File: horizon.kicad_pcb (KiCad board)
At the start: 4 copper layers, 50 x 100 mm, 242 parts, among them IC1 A3909, J1 Micro_SD_Card_Det1, J10 Conn_01x02_Pin, J11 USB_C_Receptacle_USB2.0_16P, J12 Conn_01x04, J13 1x3 servo, J14 1x3 servo, J15 arming terminal, J16 arming terminal, J17 arming terminal, J18 arming terminal, J19 Screw_Terminal_01x02, J2 Conn_02x03_Counter_Clockwise, J20 Screw_Terminal_01x02, J21 Screw_Terminal_01x02, J22 Screw_Terminal_01x02, J23 USB_C_Receptacle_USB2.0_16P, J24 USB_C_Receptacle_USB2.0_16P, J25 Conn_Coaxial, J3 Conn_Coaxial, J4 H9161TR-ND, J5 Screw_Term, J6 1x3 servo, J7 Conn_02x03_Counter_Clockwise, J8 Conn_02x03_Counter_Clockwise, J9 1x3 servo, Q1 IRLML6402, Q10 IRLML6402, Q11 IRLML6402, Q2 DMG2301L, Q3 IRLML6402, Q4 IRLML6402, Q5 IRLML6402, Q6 IRLML6402, Q7 BSS138, Q8 IRLML6402, Q9 IRLML6402, U1 MMCU, U10 LSM6DS3, U11 BGM220SC12WGA2R, U13 LTC4412xS6, U14 TPS61092, U15 AP2112K-3.3, U2 IMU, U3 NMCU, U4 TMCU, U5 LPS22HB, U6 GPS, U7 SX1276, U8 NAND, U9 TPS82130, Y1 Crystal, Y2 32.768kHz

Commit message: Added fill
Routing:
- added copper zone on B.Cu, net GND
- added copper zone on F.Cu, net GND
- added copper zone on In1.Cu, net GND
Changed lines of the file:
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@@
 		(net 315)
+	)
+	(zone
+		(net 2)
+		(net_name "GND")
+		(layers "F.Cu" "B.Cu" "In1.Cu")
+		(hatch edge 0.5)
+		(connect_pads
+			(clearance 0.5)
+		)
+		(min_thickness 0.25)
+		(filled_areas_thickness no)
+		(fill yes
+			(thermal_gap 0.5)
+			(thermal_bridge_width 0.5)
+		)
+		(polygon
+			(pts
+				(xy 76 16) (xy 126 16) (xy 126 116) (xy 76 116)
+			)
+		)
 	)
 	(embedded_fonts no)

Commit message: Started routing for BL
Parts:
- Bluetooth: renamed from U11; moved to B.Cu
- C1, C2, C3, C4, L3, R1, R2: moved to B.Cu
- SMA_BL: renamed from J25; moved to B.Cu
- SMA_GPS: renamed from J3; moved to B.Cu
- moved C20 86.4 mm to (168.3, 64.4)
- moved D2 86.4 mm to (168.2, 66.0)
- moved L1 86.4 mm to (169.3, 59.8)
- moved R11 86.4 mm to (173.5, 55.5)
- moved C4 70.6 mm to (114.0, 80.0), turned to 90 degrees
- moved L3 68.8 mm to (109.5, 79.0)
- moved GPS 64.0 mm to (151.0, 64.0), turned to -90 degrees
- moved Bluetooth 60.5 mm to (101.5, 86.5), turned to 90 degrees
- moved C3 58.6 mm to (97.5, 88.4), turned to 90 degrees
- moved U.FL_RF 56.6 mm to (211.0, 110.5), turned to -90 degrees
- moved C1 56.4 mm to (99.5, 81.6), turned to -90 degrees
- moved C2 54.8 mm to (101.0, 81.6), turned to -90 degrees
- moved R2 50.3 mm to (105.5, 83.9), turned to 90 degrees
- moved R1 49.4 mm to (106.3, 86.1)
- moved SMA_BL 48.9 mm to (101.0, 93.5), turned to -90 degrees
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- renumbered U6 to GPS, J11 to MMCU, U1 to MMCU, J23 to NMCU, U3 to NMCU, U7 to RF, J24 to TMCU, U4 to TMCU, J4 to U.FL_RF
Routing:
- net Net-(J25-In): track 0.00 -> 23.2 mm
- net Net-(U11-ANT_OUT): track 0.00 -> 11.2 mm
- net +3.3V: track 114.1 -> 120.8 mm
- net GND: track 192.9 -> 187.3 mm, vias 99 -> 96
- net Net-(D2-A): track 6.34 -> 10.9 mm, vias 0 -> 1
- net Net-(U11-DECOUPLE): track 0.00 -> 1.41 mm

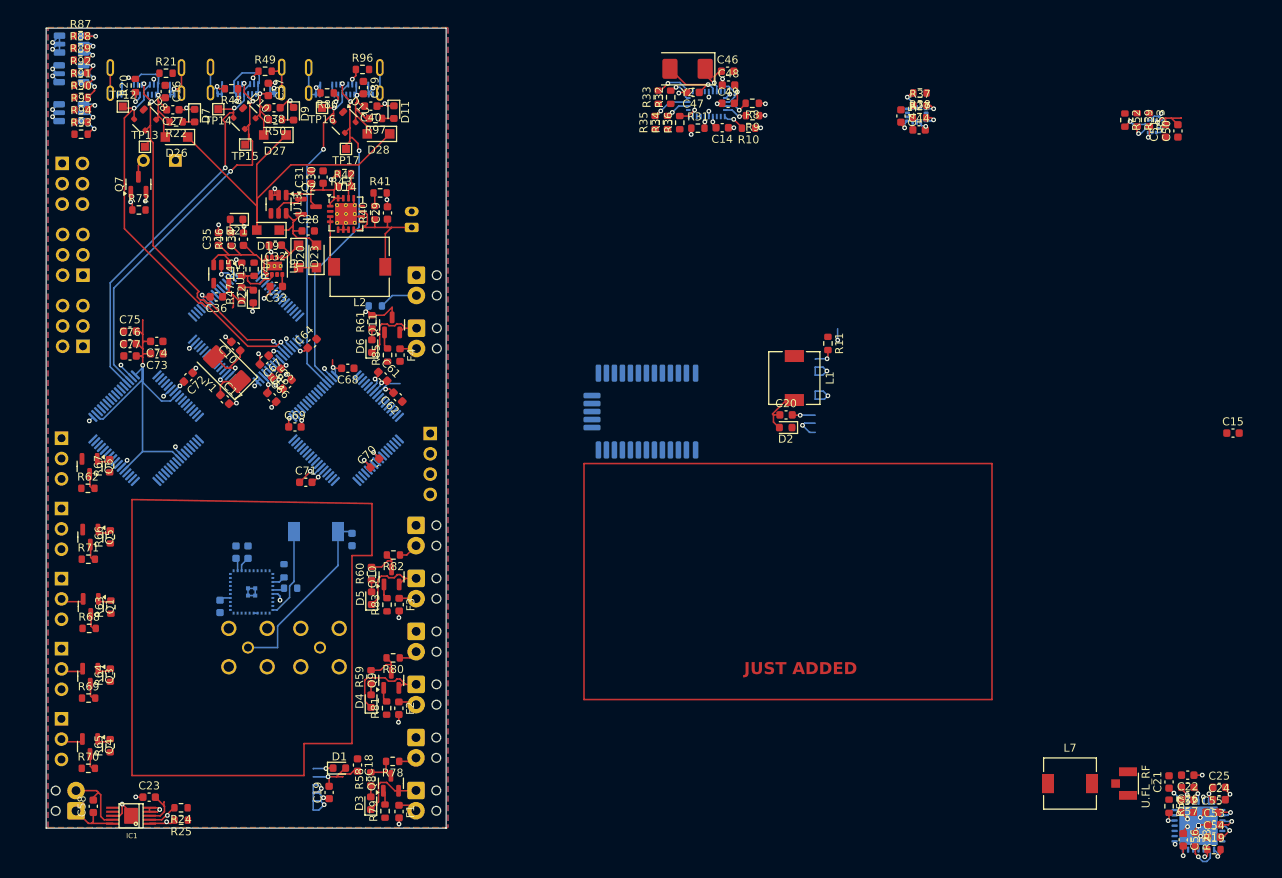
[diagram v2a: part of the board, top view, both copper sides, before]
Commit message: do some rf routing (and hopefully not break everything)
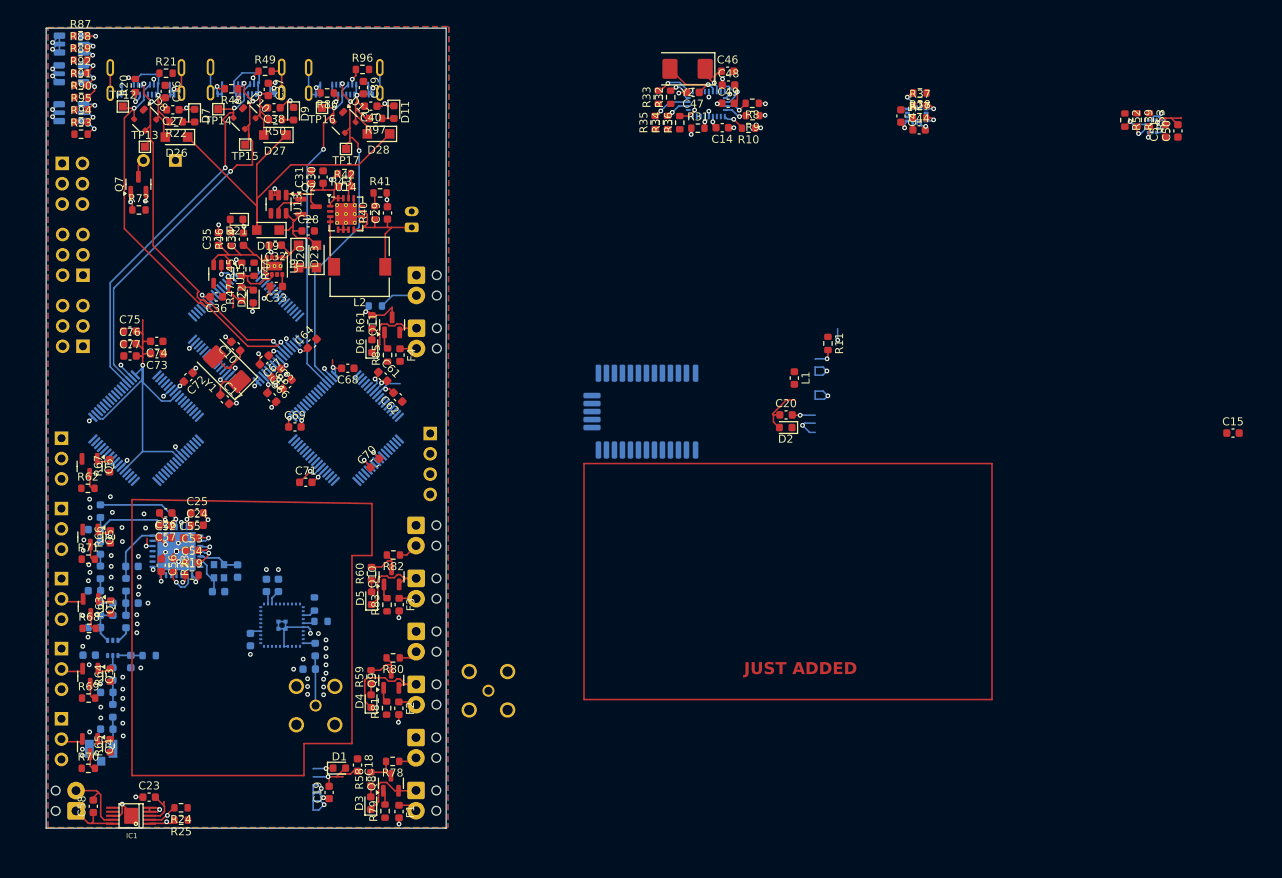
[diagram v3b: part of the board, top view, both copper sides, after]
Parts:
- removed L7: 5.6 nH, Inductor_SMD:L_6.3x6.3_H3
- removed R57: 10k, Resistor_SMD:R_0603_1608Metric
- added C11: TBD, Capacitor_SMD:C_0603_1608Metric, B.Cu at (81.8, 91.0)
- added C12: TBD, Capacitor_SMD:C_0603_1608Metric, B.Cu at (84.1, 88.7)
- added C13: TBD, Capacitor_SMD:C_0603_1608Metric, B.Cu at (86.5, 83.3)
- added C41: TBD, Capacitor_SMD:C_0603_1608Metric, B.Cu at (86.5, 88.0)
- added C42: TBD, Capacitor_SMD:C_0603_1608Metric, B.Cu at (85.8, 90.2)
- added C43: TBD, Capacitor_SMD:C_0603_1608Metric, B.Cu at (84.1, 96.8)
- added C5: TBD, Capacitor_SMD:C_0603_1608Metric, B.Cu at (97.3, 86.5)
- added C59: TBD, Capacitor_SMD:C_0603_1608Metric, B.Cu at (83.3, 99.1)
- added C6: TBD, Capacitor_SMD:C_0603_1608Metric, B.Cu at (99.7, 83.9)
- added C60: TBD, Capacitor_SMD:C_0603_1608Metric, B.Cu at (83.3, 103.7)
- added C7: TBD, Capacitor_SMD:C_0603_1608Metric, B.Cu at (81.8, 78.8)
- added C8: TBD, Capacitor_SMD:C_0603_1608Metric, B.Cu at (82.5, 81.0)
- added C9: TBD, Capacitor_SMD:C_0603_1608Metric, B.Cu at (81.8, 86.4)
- added L4: TBD, Inductor_SMD:L_0603_1608Metric, B.Cu at (82.5, 76.5)
- added L5: TBD, Inductor_SMD:L_0603_1608Metric, B.Cu at (82.5, 84.1)
- added L6: TBD, Inductor_SMD:L_0603_1608Metric, B.Cu at (82.5, 88.7)
- added L8: TBD, Inductor_SMD:L_0603_1608Metric, B.Cu at (85.8, 85.7)
- added L9: TBD, Inductor_SMD:L_0603_1608Metric, B.Cu at (84.1, 101.4)
- added R13: 1k, Resistor_SMD:R_0603_1608Metric, B.Cu at (88.7, 94.5)
- added U12: PE4259, Package_TO_SOT_SMD:SOT-363_SC-70-6, B.Cu at (84.1, 93.5)
- added Y4: 32MHz, Crystal:Crystal_SMD_Abracon_ABM10-4Pin_2.5x2.0mm, B.Cu at (97.4, 84.0)
- C21: value 2.2 pF -> 1nF; moved to B.Cu
- C22: value 1.8 pF -> 1nF; moved to B.Cu
- J25: renamed from SMA_BL; footprint SMA:LPRS_SMA_CONNECTOR -> Conn_Coaxial:LPRS_SMA_CONNECTOR
- J3: renamed from SMA_GPS; footprint SMA:LPRS_SMA_CONNECTOR -> Conn_Coaxial:LPRS_SMA_CONNECTOR
- J4: renamed from U.FL_RF; footprint U.FL:HRS_U.FL-R-SMT_01_ -> H9161TR-ND:HRS_U.FL-R-SMT_01_; moved to B.Cu
- L1, L3: footprint Inductor_SMD:L_6.3x6.3_H3 -> Inductor_SMD:L_0603_1608Metric
- U1: renamed from MMCU; footprint MK20DX256VLH7:QFP50P1200X1200X160-64N -> MMCU:QFP50P1200X1200X160-64N
- U11: renamed from Bluetooth; footprint BGM220S_SIL:BGM220SC12WGA2R -> BGM220SC12WGA2R:BGM220SC12WGA2R
- U2: footprint BNO086:IC_BNO086 -> IMU:IC_BNO086
- moved C22 138.1 mm to (81.2, 94.5)
- moved C54 132.3 mm to (94.0, 82.9)
- moved C24 132.3 mm to (94.6, 78.2)
- moved C25 132.3 mm to (94.7, 76.7)
- moved C26 132.3 mm to (90.7, 76.7)
- moved C52 132.3 mm to (90.7, 79.8)
- moved C53 132.3 mm to (94.0, 81.3)
- moved C55 132.3 mm to (93.7, 79.8)
- moved C56 132.3 mm to (90.2, 83.2)
- moved C57 132.3 mm to (90.7, 78.2)
- moved R19 132.3 mm to (94.0, 84.4)
- moved R23 132.3 mm to (91.7, 83.2)
- moved U7 132.3 mm to (92.1, 81.5)
- moved C21 130.6 mm to (86.3, 95.2), turned to -90 degrees
- moved J4 128.4 mm to (82.7, 106.2), turned to 180 degrees
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- renumbered MMCU to J11, NMCU to J23, TMCU to J24, NMCU to U3, TMCU to U4, GPS to U6, RF to U7
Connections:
- net Net-(U7-VR_PA) renamed VR_PA
- C21 pad 1: Net-(U7-RFO_HF) -> Net-(U12-CTRL)
- C21 pad 2: Net-(J4-In) -> GND
- C22 pad 1: GND -> +3.3V
- C22 pad 2: Net-(C22-Pad2) -> GND
- U4 pad 16: unconnected-(U4-PA07-Pad16) -> RF_CS
- U7 pad 16: unconnected-(U7-SCK-Pad16) -> SPI_CLOCK TMCU
- U7 pad 19: Net-(U7-NSS) -> RF_CS
- U7 pad 20: unconnected-(U7-RXTX/RF_MOD-Pad20) -> RXTX
- U7 pad 21: unconnected-(U7-RFI_HF-Pad21) -> RFI_HF
- U7 pad 22: Net-(U7-RFO_HF) -> RFO_HF
- U7 pad 5: unconnected-(U7-XTA-Pad5) -> SX_XTA
- U7 pad 6: unconnected-(U7-XTB-Pad6) -> SX_XTB
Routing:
- net Net-(J25-In): track 23.2 -> 6.23 mm
- net RFO_HF: track 0.00 -> 11.7 mm
- net VR_PA: track 3.03 -> 13.2 mm
- net Net-(U11-ANT_OUT): track 11.2 -> 1.51 mm
- net RFI_HF: track 0.00 -> 7.53 mm
- net SX_XTA: track 0.00 -> 5.22 mm
- net Net-(U12-RF1): track 0.00 -> 5.04 mm
- net SX_XTB: track 0.00 -> 4.97 mm
- net Net-(C12-Pad1): track 0.00 -> 4.60 mm
- net Net-(J4-In): track 0.00 -> 3.97 mm
- net GND: track 187.3 -> 190.8 mm, vias 96 -> 156
- net Net-(U12-CTRL): track 0.00 -> 3.10 mm
- net Net-(C43-Pad2): track 0.00 -> 3.06 mm
- net Net-(C41-Pad1): track 0.00 -> 3.06 mm
- net Net-(U7-RFO_HF): track 2.44 -> 0.00 mm, vias 1 -> 0
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- added copper zone on In1.Cu, net +3.3V
- added copper zone on In2.Cu, net GND

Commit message: pcb layout done
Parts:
- moved U8 183.9 mm to (92.8, 89.1)
- moved J1 164.7 mm to (110.1, 86.4)
- moved R54 149.2 mm to (91.2, 90.0), turned to 90 degrees
- moved R53 146.0 mm to (87.3, 100.6), turned to 0 degrees
- moved C50 145.5 mm to (88.7, 97.0), turned to 180 degrees
- moved R39 145.5 mm to (87.3, 102.1), turned to 0 degrees
- moved U5 145.0 mm to (88.1, 100.3), turned to -90 degrees
- moved R52 144.9 mm to (87.3, 103.7), turned to 0 degrees
- moved C51 144.9 mm to (88.7, 98.6), turned to 180 degrees
- moved R12 143.4 mm to (94.8, 90.5), turned to 90 degrees
- moved R55 133.5 mm to (106.7, 89.6)
- moved C15 133.3 mm to (92.4, 87.3)
- moved R56 125.8 mm to (114.5, 81.1)
- moved R38 125.4 mm to (95.2, 111.8), turned to -90 degrees
- moved R37 123.2 mm to (96.8, 111.8), turned to 90 degrees
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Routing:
- net GND: track 190.8 -> 216.7 mm, vias 156 -> 158
- net Net-(D2-A): track 10.9 -> 15.4 mm, vias 1 -> 0
- net CS_SD MMCU: track 0.00 -> 3.03 mm, vias 0 -> 1
- net Net-(U11-DECOUPLE): track 1.41 -> 3.97 mm
- net Net-(U8-~{HOLD}/~{RESET}/IO_{3}): track 0.00 -> 2.44 mm, vias 0 -> 1
- net SD_DETECT: track 0.00 -> 2.30 mm, vias 0 -> 1
- net Net-(U8-~{WP}/IO_{2}): track 0.00 -> 2.20 mm, vias 0 -> 1
- net +3.3V: track 121.2 -> 119.2 mm, vias 19 -> 20
- net SX_XTB: track 4.97 -> 5.78 mm
- removed copper zone on B.Cu, net GND
- removed copper zone on F.Cu, net GND
- removed copper zone on In1.Cu, net GND
- removed copper zone on In2.Cu, net GND
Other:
- board text removed: "JUST ADDED"

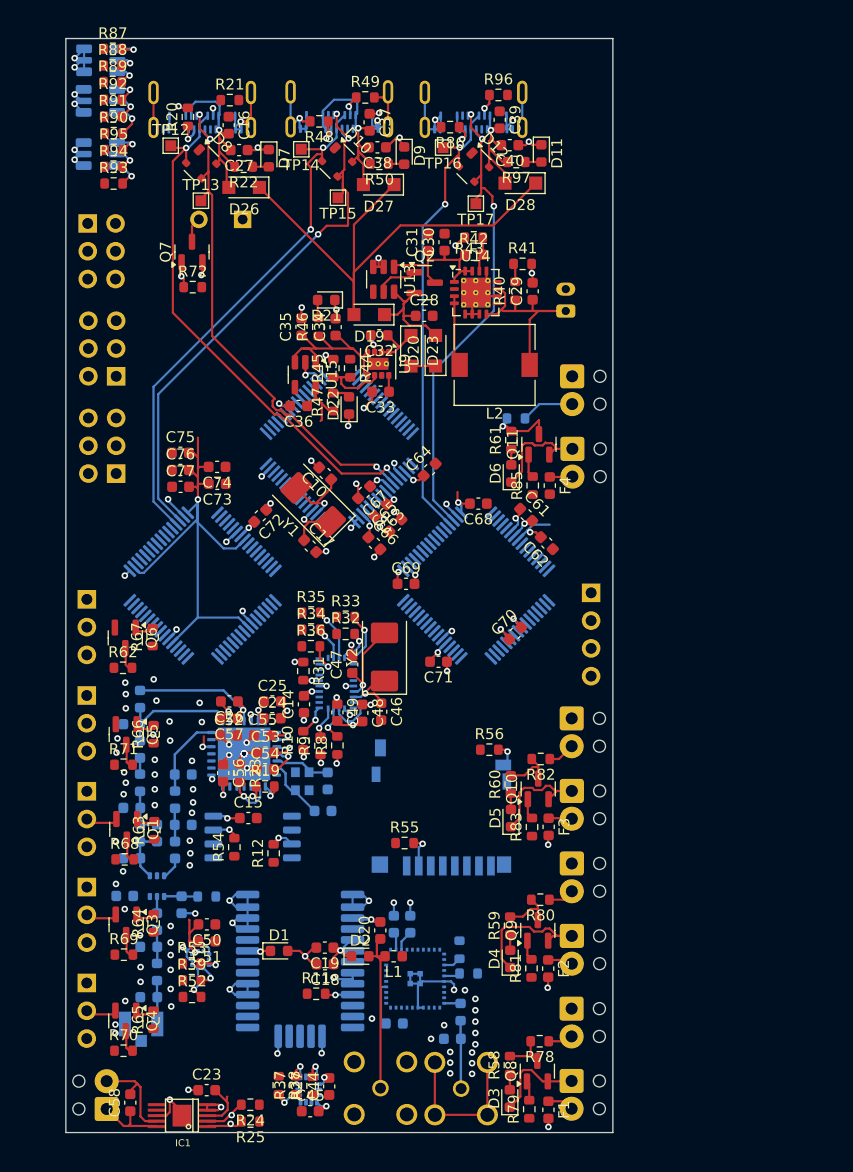
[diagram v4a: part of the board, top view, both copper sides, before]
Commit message: new usb, move micro sd, redo boost converter (pls find a place on the pcb tomorrow)
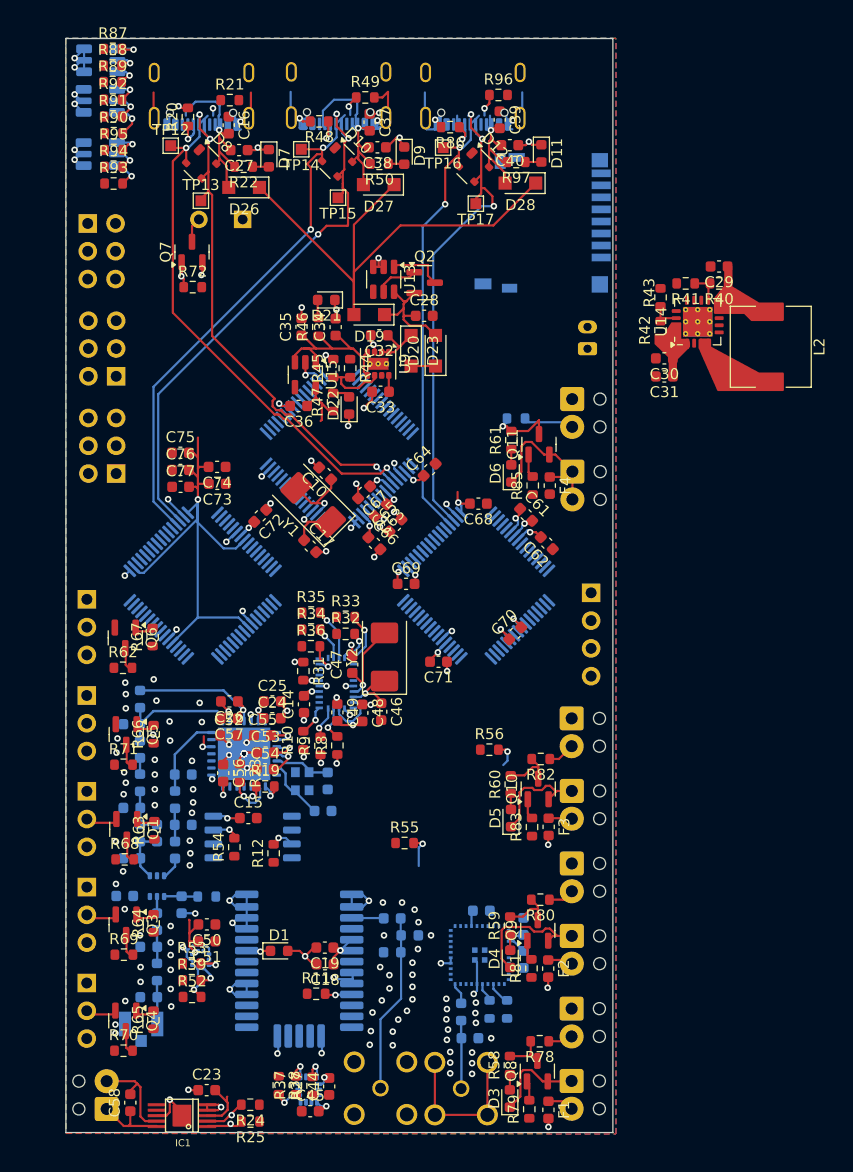
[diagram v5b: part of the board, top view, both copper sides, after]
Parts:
- C20, D2, L1: moved to B.Cu
- J11, J23, J24: footprint Connector_USB:USB_C_Receptacle_Amphenol_124019772112A -> Connector_USB:USB_C_Receptacle_GCT_USB4105-xx-A_16P_TopMnt_Horizontal
- moved J1 54.2 mm to (119.3, 32.9), turned to -90 degrees
- moved L2 25.3 mm to (140.2, 44.2), turned to -90 degrees
- moved C31 24.9 mm to (130.5, 47.0), turned to 180 degrees
- moved C30 22.7 mm to (130.5, 45.3), turned to 180 degrees
- moved U14 20.5 mm to (133.5, 42.0), turned to 90 degrees
- moved R40 18.6 mm to (135.5, 38.5), turned to 180 degrees
- moved R42 18.4 mm to (130.1, 42.7), turned to 90 degrees
- moved R43 17.9 mm to (130.1, 39.7), turned to 90 degrees
- moved C29 17.2 mm to (135.5, 36.9), turned to 180 degrees
- moved R41 15.0 mm to (132.4, 38.5), turned to 180 degrees
- moved C3 13.0 mm to (113.8, 95.8)
- moved C1 11.8 mm to (117.6, 97.2)
- moved C2 10.8 mm to (117.6, 100.2), turned to 90 degrees
- moved U11 6.28 mm to (113.6, 99.8), turned to 0 degrees
- moved R2 6.11 mm to (114.5, 104.8), turned to -90 degrees
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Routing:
- net GND: track 216.7 -> 198.0 mm, vias 158 -> 177
- net Net-(J10-Pin_1): track 17.3 -> 1.51 mm
- net Net-(L2-Pad2): track 6.47 -> 0.00 mm
- net bat: track 14.2 -> 8.57 mm
- net Net-(U11-DECOUPLE): track 3.97 -> 1.45 mm
- net Net-(J22-Pin_2): track 2.08 -> 4.10 mm
- net +3.3V: track 119.2 -> 117.3 mm
- net Net-(J24-CC1): track 2.48 -> 3.83 mm
- net Net-(D12-VCC): track 13.8 -> 12.4 mm
- net Net-(U14-LBI): track 1.71 -> 3.00 mm
- net Net-(D2-A): track 15.4 -> 16.3 mm
- net D- DMCU-2: track 45.3 -> 45.9 mm
- net Net-(U6-RF_OUT): track 2.68 -> 2.95 mm, vias 1 -> 0
- added copper zone on B.Cu, net GND
- added copper zone on F.Cu, net GND
- added copper zone on In1.Cu, net GND
- added copper zone on In2.Cu, net GND
- removed copper zone on In1.Cu, net +3.3V
